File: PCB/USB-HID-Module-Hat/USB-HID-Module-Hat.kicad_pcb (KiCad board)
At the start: 2 copper layers, 21 parts, among them J1 RJHSE-5381, J2 Raspberry_Pi_2_3, U1 MAX3535ECWI+T

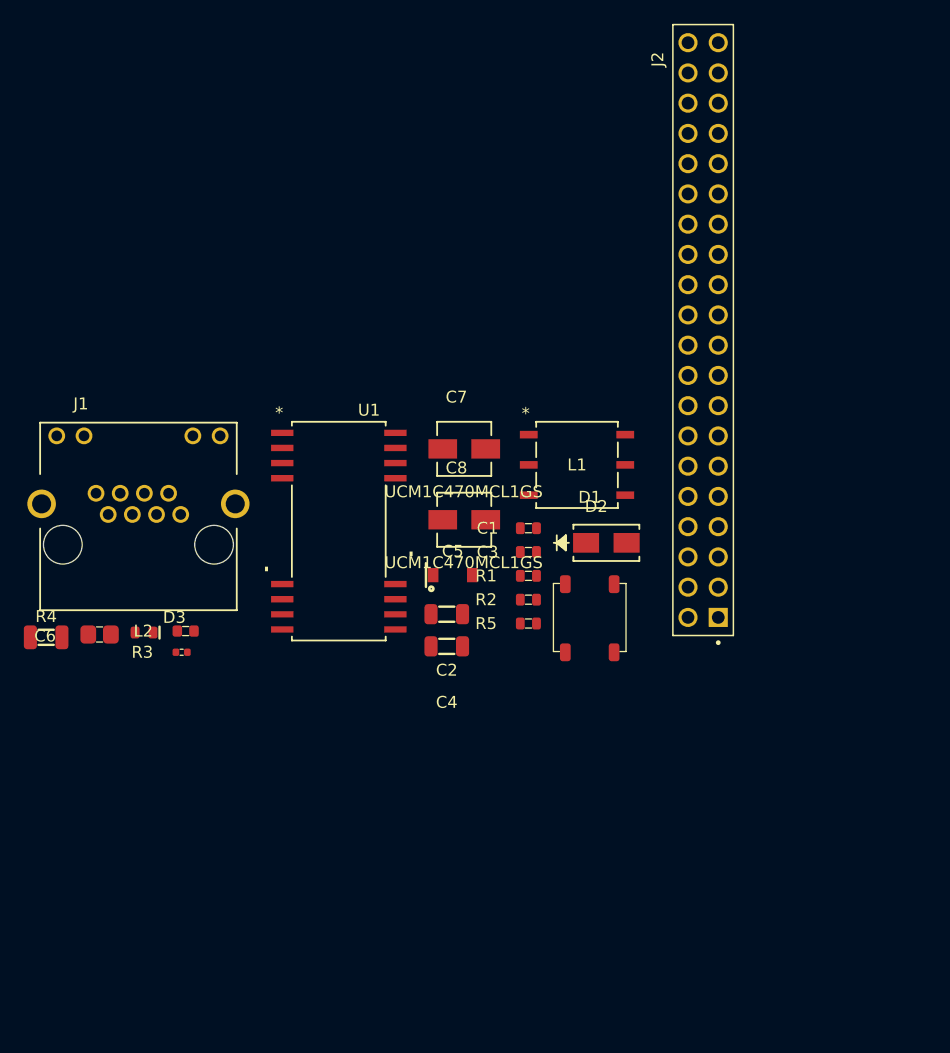
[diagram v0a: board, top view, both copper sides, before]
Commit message: PCB
PCB layout 80% complete. Board shape defined. Components and connectors places !
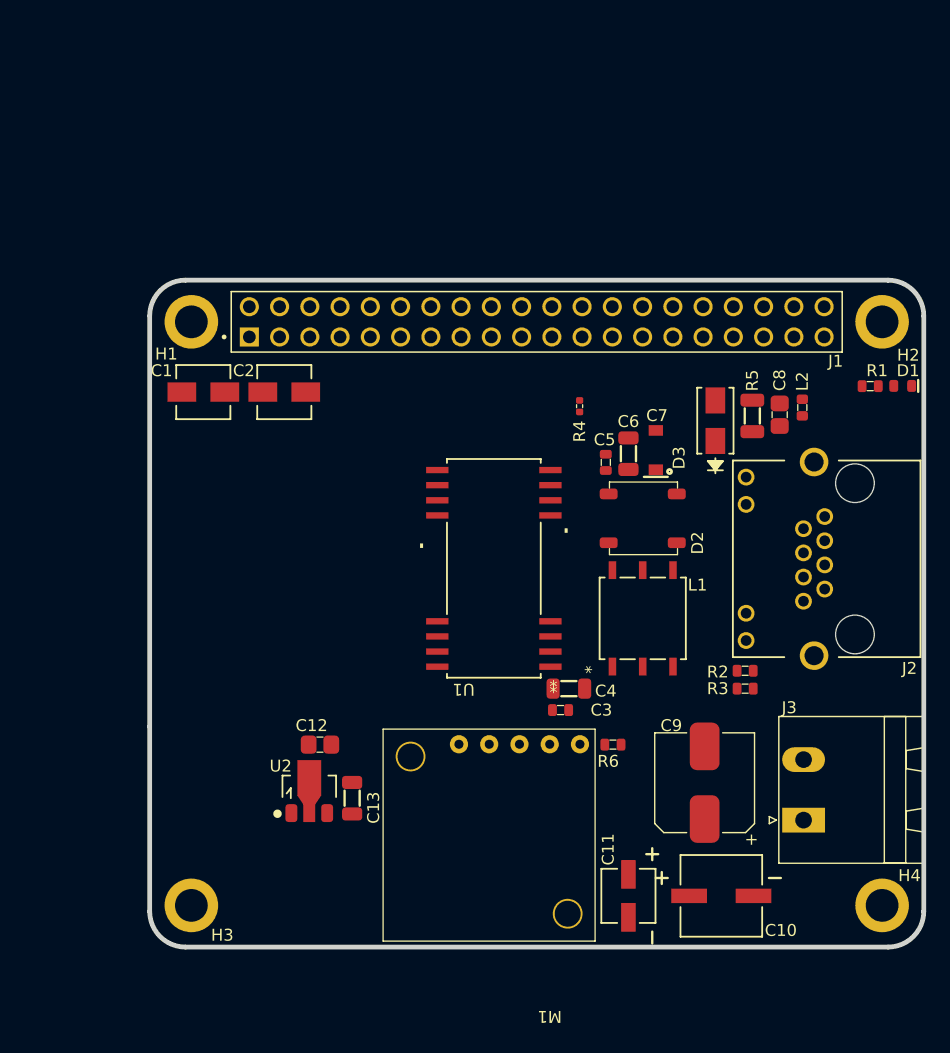
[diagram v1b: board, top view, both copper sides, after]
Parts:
- added C10: UUQ1H100MCL1GB, AVR-KiCAD-Lib-Capacitors:CAP_UUQ_6P3X5P4_NCH, F.Cu at (158.0, 101.7)
- added C11: UUQ1H010MCL1GB, AVR-KiCAD-Lib-Capacitors:CAP_UUQ_4X5P4_NCH, F.Cu at (150.2, 101.7)
- added C12: GRM21BR61A226ME51L, AVR-KiCAD-Lib-Capacitors:C0805, F.Cu at (124.3, 89.0)
- added C13: GRT31CR61H106KE01L, AVR-KiCAD-Lib-Capacitors:C1206, F.Cu at (127.0, 93.5)
- added C9: UUQ1H470MCL1GS, AVR-KiCAD-Lib-Capacitors:CP_Elec_8x10, F.Cu at (156.6, 92.2)
- added H1: MountingHole_Pad, AVR-KiCAD-Lib-Holes_Fasteners:RPI_HAT_HOLE, F.Cu at (113.5, 53.5)
- added H2: MountingHole_Pad, AVR-KiCAD-Lib-Holes_Fasteners:RPI_HAT_HOLE, F.Cu at (171.5, 53.5)
- added H3: MountingHole_Pad, AVR-KiCAD-Lib-Holes_Fasteners:RPI_HAT_HOLE, F.Cu at (113.5, 102.5)
- added H4: MountingHole_Pad, AVR-KiCAD-Lib-Holes_Fasteners:RPI_HAT_HOLE, F.Cu at (171.5, 102.5)
- added J3: 1757242, AVR-KiCAD-Lib-Connectors:PhoenixContact_MSTBA-G_02x5.08mm_Angled, F.Cu at (164.9, 95.3)
- added M1: D24V22F5, AVR-KiCAD-Lib-Modules:D24V22F12, F.Cu at (146.1, 89.0)
- added R6: RC0603FR-072K2L, AVR-KiCAD-Lib-Resistors:R0603, F.Cu at (148.9, 89.0)
- added U2: AZ1117CR-3.3TRG1, AVR-KiCAD-Lib-ICs:SOT_89, F.Cu at (123.4, 92.9)
- C1: value CL10B104JB8NNNC -> UCM1C470MCL1GS; footprint AVR-KiCAD-Lib-Capacitors:C0603 -> AVR-KiCAD-Lib-Capacitors:UCM1C470MCL1GS
- C2: value CGA5L3X5R1V106K160AB -> UCM1C470MCL1GS; footprint AVR-KiCAD-Lib-Capacitors:C1206 -> AVR-KiCAD-Lib-Capacitors:UCM1C470MCL1GS
- C5: value C1206C105K3RACAUTO -> CL10B104JB8NNNC; footprint AVR-KiCAD-Lib-Diodes:D_SOD-123 -> AVR-KiCAD-Lib-Capacitors:C0603
- C6: value C0805C103KCRACAUTO -> CGA5L3X5R1V106K160AB; footprint AVR-KiCAD-Lib-Capacitors:C0805 -> AVR-KiCAD-Lib-Capacitors:C1206
- C7: value UCM1C470MCL1GS -> C1206C105K3RACAUTO; footprint AVR-KiCAD-Lib-Capacitors:UCM1C470MCL1GS -> AVR-KiCAD-Lib-Diodes:D_SOD-123
- C8: value UCM1C470MCL1GS -> C0805C103KCRACAUTO; footprint AVR-KiCAD-Lib-Capacitors:UCM1C470MCL1GS -> AVR-KiCAD-Lib-Capacitors:C0805
- D1: value LMB110S-TP -> LTST-C194KGKT; footprint AVR-KiCAD-Lib-Diodes:LMB110S-TP -> AVR-KiCAD-Lib-Diodes:LED0603
- D2: value SMAJ30CA -> LMB110S-TP; footprint AVR-KiCAD-Lib-Diodes:SMAJ30CA -> AVR-KiCAD-Lib-Diodes:LMB110S-TP
- D3: value LTST-C194KGKT -> SMAJ30CA; footprint AVR-KiCAD-Lib-Diodes:LED0603 -> AVR-KiCAD-Lib-Diodes:SMAJ30CA
- J1: value RJHSE-5381 -> Raspberry_Pi_2_3; footprint AVR-KiCAD-Lib-Connectors:AMPHENOL_RJHSE-5381 -> AVR-KiCAD-Lib-Connectors:SULLINS_PPPC202LFBN-RC_RPi5
- J2: value Raspberry_Pi_2_3 -> RJHSE-5381; footprint AVR-KiCAD-Lib-Connectors:SULLINS_PPPC202LFBN-RC_RPi5 -> AVR-KiCAD-Lib-Connectors:AMPHENOL_RJHSE-5381
- R3: value AC0402FR-07120RL -> RC0603FR-07470RL; footprint AVR-KiCAD-Lib-Resistors:R0402 -> AVR-KiCAD-Lib-Resistors:R0603
- R4: value RC1206FR-071ML -> AC0402FR-07120RL; footprint AVR-KiCAD-Lib-Resistors:R1206 -> AVR-KiCAD-Lib-Resistors:R0402
- R5: value RC0603FR-07470RL -> RC1206FR-071ML; footprint AVR-KiCAD-Lib-Resistors:R0603 -> AVR-KiCAD-Lib-Resistors:R1206
- moved L2 55.1 mm to (164.8, 60.7), turned to 90 degrees
- moved D3 51.2 mm to (157.5, 61.8), turned to 90 degrees
- moved R4 48.8 mm to (146.1, 60.6), turned to 90 degrees
- moved R3 47.4 mm to (160.0, 84.3), turned to 180 degrees
- moved C6 46.9 mm to (150.2, 64.6), turned to -90 degrees
- moved J1 38.3 mm to (142.5, 53.5), turned to 180 degrees
- moved R1 32.8 mm to (170.5, 58.9), turned to 180 degrees
- moved D1 32.7 mm to (173.2, 58.9)
- moved C1 29.6 mm to (114.5, 59.4), turned to 180 degrees
- moved C8 27.9 mm to (162.9, 61.3), turned to 90 degrees
- moved R5 25.6 mm to (160.6, 61.4), turned to -90 degrees
- moved C2 23.1 mm to (121.3, 59.4)
- moved J2 23.1 mm to (169.2, 73.4), turned to 90 degrees
- moved R2 19.2 mm to (160.0, 82.8), turned to 180 degrees
- moved C7 16.1 mm to (152.5, 64.3), turned to 90 degrees
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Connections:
- C1 pad 1: GND -> +5V
- C1 pad 2: +3.3V -> GND
- C2 pad 1: GND -> +5V
- C2 pad 2: +3.3V -> GND
- C3 pad 1: Earth -> GND
- C3 pad 2: +5V -> +3.3V
- C4 pad 1: Earth -> GND
- C4 pad 2: +5V -> +3.3V
- C6 pad 1: /RJ45_SHIELD -> Earth
- C6 pad 2: GND -> +5V
- C7 pad 1: +5V -> Earth
- C7 pad 2: GND -> +5V
- C8 pad 1: +5V -> /RS485/RJ45_SHIELD
- D1 pad 2: Net-(D1-Pad2) -> GND
- D2 pad 1: /RJ45_SHIELD -> Net-(D2-Pad1)
- D2 pad 2: GND -> Net-(D2-Pad2)
- D3 pad 1: Net-(D3-Pad1) -> /RS485/RJ45_SHIELD
- J1 pad 1: /A_RS485 -> unconnected-(J1-3V3-Pad1)
- J1 pad 10: Net-(J1-Pad10) -> Net-(J1-GPIO15/RXD)
- J1 pad 11: GND -> Net-(J1-GPIO17)
- J1 pad 12: Net-(J1-Pad12) -> Net-(J1-GPIO18/PWM0)
- J1 pad 2: /B_RS485 -> +5V
- J1 pad 4: unconnected-(J1-Pad4) -> +5V
- J1 pad 6: unconnected-(J1-Pad6) -> GND
- J1 pad 7: /Y_RS485 -> unconnected-(J1-GCLK0/GPIO4-Pad7)
- J1 pad 8: /Z_RS485 -> Net-(J1-GPIO14/TXD)
- J2 pad 1: unconnected-(J2-3V3-Pad1) -> /RS485/A_RS485
- J2 pad 10: Net-(J2-GPIO15/RXD) -> Net-(J2-Pad10)
- J2 pad 11: Net-(J2-GPIO17) -> GND
- J2 pad 12: Net-(J2-GPIO18/PWM0) -> Net-(J2-Pad12)
- J2 pad 2: +5V -> /RS485/B_RS485
- J2 pad 4: +5V -> unconnected-(J2-Pad4)
- J2 pad 6: GND -> unconnected-(J2-Pad6)
- J2 pad 7: unconnected-(J2-GCLK0/GPIO4-Pad7) -> /RS485/Y_RS485
- J2 pad 8: Net-(J2-GPIO14/TXD) -> /RS485/Z_RS485
- L1 pad 4: Net-(D1-Pad1) -> Net-(D2-Pad1)
- L1 pad 6: Net-(D1-Pad2) -> Net-(D2-Pad2)
- L2 pad 1: /RJ45_SHIELD -> /RS485/RJ45_SHIELD
- R1 pad 1: Net-(J1-Pad12) -> Net-(D1-Pad1)
- R1 pad 2: Net-(J2-GPIO22) -> Net-(J1-PWM1/GPIO13)
- R2 pad 1: Net-(J1-Pad10) -> Net-(J2-Pad12)
- R2 pad 2: Net-(J2-GPIO23) -> Net-(J1-GPIO22)
- R3 pad 1: /A_RS485 -> Net-(J2-Pad10)
- R3 pad 2: /B_RS485 -> Net-(J1-GPIO23)
- R4 pad 1: GND -> /RS485/A_RS485
- R4 pad 2: /RJ45_SHIELD -> /RS485/B_RS485
- R5 pad 1: Net-(D3-Pad1) -> GND
- R5 pad 2: Net-(J2-PWM1/GPIO13) -> /RS485/RJ45_SHIELD
- U1 pad 12: /Z_RS485 -> /RS485/Z_RS485
- U1 pad 13: /Y_RS485 -> /RS485/Y_RS485
- U1 pad 15: /B_RS485 -> /RS485/B_RS485
- U1 pad 16: /A_RS485 -> /RS485/A_RS485
- U1 pad 25: Net-(J2-GPIO14/TXD) -> Net-(J1-GPIO14/TXD)
- U1 pad 26: Net-(J2-GPIO18/PWM0) -> Net-(J1-GPIO18/PWM0)
- U1 pad 27: Net-(J2-GPIO17) -> Net-(J1-GPIO17)
- U1 pad 28: Net-(J2-GPIO15/RXD) -> Net-(J1-GPIO15/RXD)
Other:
- board outline added: 65 x 56 mm

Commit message: First Pass at PCB
PCB layout completed, pending design review.
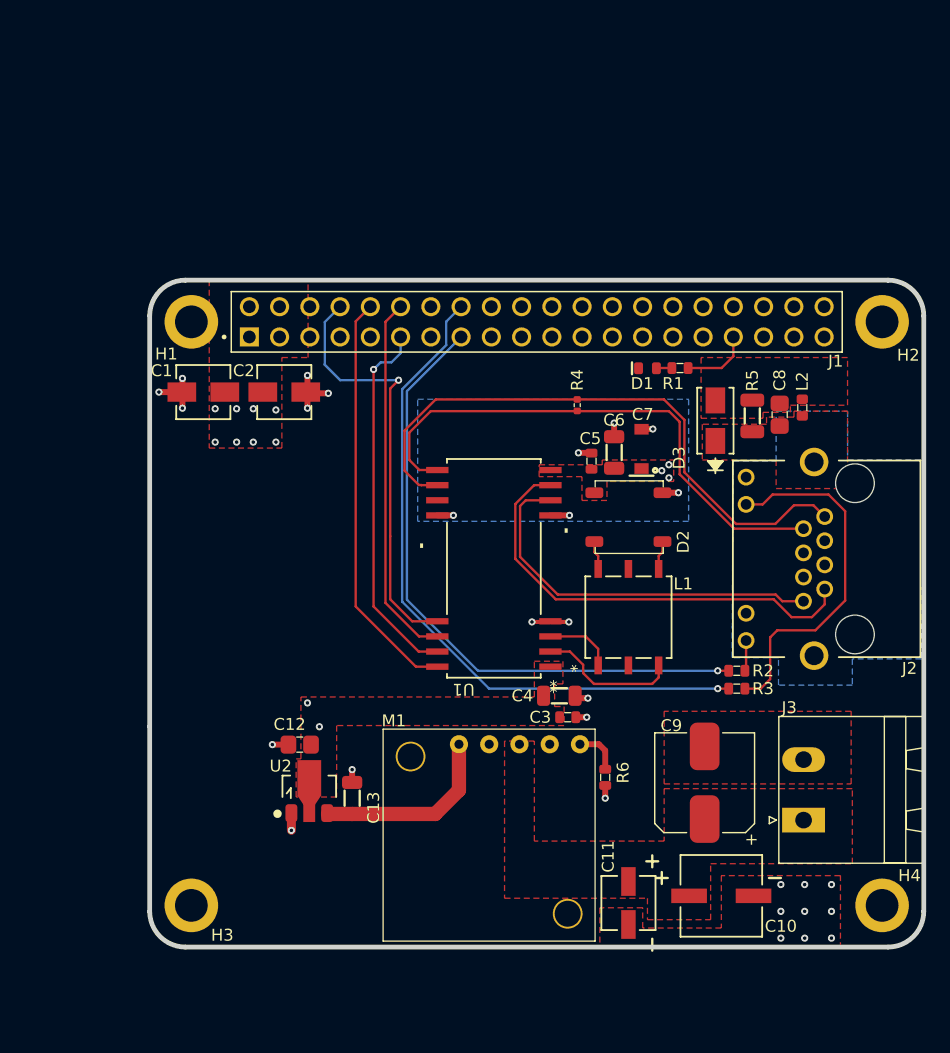
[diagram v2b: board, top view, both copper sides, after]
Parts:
- moved D1 21.5 mm to (151.8, 57.4), turned to 180 degrees
- moved R1 16.0 mm to (154.5, 57.4), turned to 0 degrees
- moved R6 2.83 mm to (148.2, 91.8), turned to -90 degrees
- moved C12 1.70 mm to (122.6, 89.0), turned to 0 degrees
- moved L1 1.20 mm to (150.2, 78.3)
- moved C5 1.20 mm to (147.1, 65.2)
- moved D2 1.20 mm to (150.2, 69.9)
- moved C6 1.20 mm to (149.0, 64.5)
- moved C7 1.20 mm to (151.3, 64.2)
- moved C4 1.00 mm to (144.4, 84.9)
- moved C3 0.85 mm to (145.1, 86.7)
- moved R2 0.70 mm to (159.3, 82.8)
- moved R3 0.70 mm to (159.3, 84.3)
- moved C11 0.60 mm to (150.2, 102.3)
- moved R4 0.22 mm to (145.9, 60.5), turned to -90 degrees
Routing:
- net Net-(J1-GPIO23): track 0.00 -> 57.3 mm, vias 0 -> 1
- net Net-(J1-GPIO22): track 0.00 -> 53.4 mm, vias 0 -> 1
- net /RS485/A_RS485: track 0.00 -> 50.9 mm
- net /RS485/B_RS485: track 0.00 -> 45.5 mm
- net /RS485/Y_RS485: track 0.00 -> 37.9 mm
- net Net-(J1-GPIO14/TXD): track 0.00 -> 35.5 mm, vias 0 -> 1
- net Net-(J1-GPIO15/RXD): track 0.00 -> 34.6 mm
- net /RS485/Z_RS485: track 0.00 -> 32.4 mm
- net Net-(J1-GPIO17): track 0.00 -> 31.0 mm, vias 0 -> 1
- net Net-(J1-GPIO18/PWM0): track 0.00 -> 30.9 mm
- net Net-(J2-Pad10): track 0.00 -> 30.3 mm
- net GND: track 0.00 -> 18.4 mm, vias 0 -> 22
- net +5V: track 0.00 -> 15.8 mm, vias 0 -> 11
- net Net-(U1-ST1): track 0.00 -> 11.9 mm
- net Earth: track 0.00 -> 7.51 mm, vias 0 -> 6
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- added copper zone on F.Cu, net +24V
- added copper zone on F.Cu, net +3.3V
- added copper zone on In2.Cu, net +3.3V
- added copper zone on F.Cu, net +5V
- added copper zone on In2.Cu, net +5V
- added copper zone on B.Cu, net /RS485/RJ45_SHIELD
- added copper zone on F.Cu, net /RS485/RJ45_SHIELD
- added copper zone on B.Cu, net Earth
- added copper zone on F.Cu, net GND
- added copper zone on In1.Cu, net GND
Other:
- copper layers 2 -> 4
